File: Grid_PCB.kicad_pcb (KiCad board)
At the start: 2 copper layers, 220 x 20 mm, 31 parts, among them J1 Conn_01x04_Female, J10 LED_Conn, J2 Conn_01x04_Female, J3 Conn_01x04_Female, J4 Conn_01x04_Female, J5 Conn_01x04_Female, J6 Conn_01x04_Female, J7 Conn_01x04_Female, J8 Conn_01x04_Female, J9 ESP_Conn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

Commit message: continued progress
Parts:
- added H1: MountingHole, MountingHole:MountingHole_3.2mm_M3, F.Cu at (179.1, 15.2)
- added H1: MountingHole, MountingHole:MountingHole_3.2mm_M3, F.Cu at (54.6, 3.81)
- moved H2 89.6 mm to (207.0, 3.81)
- moved H1 66.3 mm to (29.2, 15.2)
- moved RN1 64.1 mm to (126.6, 2.54)
- moved J10 13.6 mm to (226.1, 15.5), turned to 0 degrees
- moved C8 9.71 mm to (222.0, 15.2)
- moved J8 9.47 mm to (217.2, 8.73)
- moved D8 9.45 mm to (222.2, 10.2)
- moved J9 8.13 mm to (2.54, 19.1)
- moved TP1 7.62 mm to (22.9, 3.81)
- moved U1 7.62 mm to (19.1, 19.1)
- moved C7 5.36 mm to (196.8, 15.2)
- moved C4 5.35 mm to (120.4, 15.2)
- moved D7 4.99 mm to (196.8, 10.2)
- moved J7 4.70 mm to (191.8, 8.73)
- moved C6 2.60 mm to (171.2, 15.2)
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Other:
- board size 220 x 20 mm -> 228.2 x 20 mm

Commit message: finished first pass at routing
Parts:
- removed the H1 at (179.1, 15.2)
- removed the H1 at (54.6, 3.81)
- removed the H1 at (29.2, 15.2)
- removed RN1: R_Network08(10k), Resistor_THT:R_Array_SIP9
- added H1: MountingHole, MountingHole:MountingHole_3.2mm_M3, F.Cu at (66.8, 88.1)
- added H3: MountingHole, MountingHole:MountingHole_3.2mm_M3, F.Cu at (219.5, 99.6)
- added H4: MountingHole, MountingHole:MountingHole_3.2mm_M3, F.Cu at (244.6, 88.1)
- added R1: 10K, Resistor_SMD:R_0805_2012Metric_Pad1.20x1.40mm_HandSolder, F.Cu at (75.9, 89.4)
- added R2: 10K, Resistor_SMD:R_0805_2012Metric_Pad1.20x1.40mm_HandSolder, F.Cu at (101.3, 89.7)
- added R3: 10K, Resistor_SMD:R_0805_2012Metric_Pad1.20x1.40mm_HandSolder, F.Cu at (126.7, 89.4)
- added R4: 10K, Resistor_SMD:R_0805_2012Metric_Pad1.20x1.40mm_HandSolder, F.Cu at (152.1, 89.4)
- added R5: 10K, Resistor_SMD:R_0805_2012Metric_Pad1.20x1.40mm_HandSolder, F.Cu at (177.5, 89.3)
- added R6: 10K, Resistor_SMD:R_0805_2012Metric_Pad1.20x1.40mm_HandSolder, F.Cu at (202.9, 89.4)
- added R7: 10K, Resistor_SMD:R_0805_2012Metric_Pad1.20x1.40mm_HandSolder, F.Cu at (228.3, 89.4)
- added R8: 10K, Resistor_SMD:R_0805_2012Metric_Pad1.20x1.40mm_HandSolder, F.Cu at (253.7, 89.4)
- J9: footprint Connector_PinHeader_2.54mm:PinHeader_1x08_P2.54mm_Horizontal -> Connector_PinHeader_2.54mm:PinHeader_1x07_P2.54mm_Horizontal
- moved H2 149.7 mm to (91.9, 99.6)
- moved C8 92.1 mm to (260.1, 99.1)
- moved D6 92.1 mm to (209.6, 94.0)
- moved D8 92.1 mm to (260.4, 94.0)
- moved C1 92.1 mm to (82.3, 99.1)
- moved C3 92.1 mm to (133.3, 99.1)
- moved C4 92.1 mm to (158.5, 99.1)
- moved C5 92.1 mm to (184.2, 99.1)
- moved C6 92.1 mm to (209.3, 99.1)
- moved C7 92.1 mm to (234.9, 99.1)
- moved D1 92.1 mm to (82.5, 94.0)
- moved D2 92.1 mm to (108.0, 94.0)
- moved D3 92.1 mm to (133.3, 94.0)
- moved D4 92.1 mm to (158.8, 94.0)
- moved D5 92.1 mm to (184.2, 94.0)
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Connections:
- J10 pad 1: /LED_Out -> /LED_In
- J10 pad 2: /LED_In -> /LED_Out
- J9 pad 2: /MUX_OUT -> /ESPselC
- J9 pad 3: /ESPselA -> /ESPselB
- J9 pad 4: /ESPselB -> /ESPselA
- J9 pad 5: /ESPselC -> /MUX_OUT
- U1 pad 13: /BTN5 -> /BTN6
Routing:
- net VDD: track 0.00 -> 273.0 mm
- net /LED_In: track 0.00 -> 228.6 mm, vias 0 -> 3
- net /BTN7: track 0.00 -> 212.1 mm
- net /BTN6: track 0.00 -> 183.8 mm
- net /BTN5: track 0.00 -> 155.5 mm
- net /BTN4: track 0.00 -> 127.3 mm
- net /BTN3: track 0.00 -> 95.8 mm
- net /BTN2: track 0.00 -> 73.7 mm
- net /BTN1: track 0.00 -> 50.9 mm
- net /BTN0: track 0.00 -> 28.0 mm
- net /InputNode7/DIN: track 0.00 -> 25.5 mm, vias 0 -> 2
- net /InputNode6/DIN: track 0.00 -> 25.5 mm, vias 0 -> 2
- net /InputNode2/DIN: track 0.00 -> 25.5 mm, vias 0 -> 2
- net /LED_Link: track 0.00 -> 25.4 mm, vias 0 -> 2
- net /InputNode3/DIN: track 0.00 -> 25.4 mm, vias 0 -> 2
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- added copper zone on B.Cu, net GND
- added copper zone on F.Cu, net GND
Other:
- outline, holes or cut-outs redrawn
- net class Power added: clearance 0.2, trace_width 0.5, via_dia 0.8, via_drill 0.4

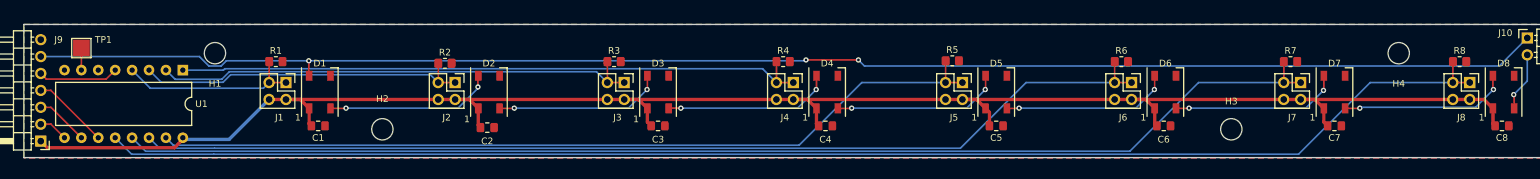
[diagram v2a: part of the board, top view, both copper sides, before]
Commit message: trace update
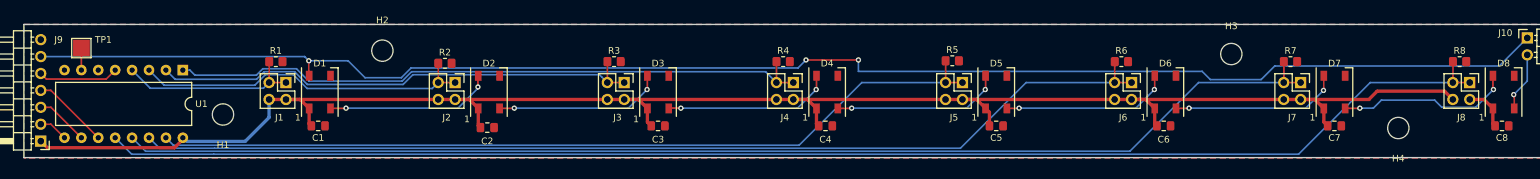
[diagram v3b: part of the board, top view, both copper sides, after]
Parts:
- moved H2 11.8 mm to (91.9, 87.8)
- moved H3 11.3 mm to (219.5, 88.3)
- moved H4 11.2 mm to (244.5, 99.4)
- moved H1 9.29 mm to (68.0, 97.3)
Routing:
- net /LED_In: track 228.6 -> 232.9 mm
- net /BTN3: track 95.8 -> 97.6 mm
- net /BTN2: track 73.7 -> 74.9 mm
- net /BTN1: track 50.9 -> 52.0 mm
- net /InputNode7/DIN: track 25.5 -> 26.6 mm

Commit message: flipped components to back side
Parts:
- removed TP1: TestPoint, TestPoint:TestPoint_Pad_2.5x2.5mm
- added J11: ESP_Conn, Connector_JST:JST_EH_B2B-EH-A_1x02_P2.50mm_Vertical, B.Cu at (46.3, 101.4)
- J10: footprint Connector_PinHeader_2.54mm:PinHeader_1x02_P2.54mm_Horizontal -> Connector_JST:JST_EH_B2B-EH-A_1x02_P2.50mm_Vertical; moved to B.Cu
- J9: footprint Connector_PinHeader_2.54mm:PinHeader_1x07_P2.54mm_Horizontal -> Connector_JST:JST_EH_B5B-EH-A_1x05_P2.50mm_Vertical; moved to B.Cu
- U1: moved to B.Cu
- moved U1 17.3 mm to (45.0, 87.4)
- moved J9 4.37 mm to (41.1, 97.0), turned to 90 degrees
- moved J10 3.97 mm to (260.1, 87.1)
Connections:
- J9 pad 1: VDD -> /ESPselA
- J9 pad 2: /ESPselC -> /ESPselB
- J9 pad 3: /ESPselB -> /ESPselC
- J9 pad 4: /ESPselA -> /MUX_OUT
- J9 pad 5: /MUX_OUT -> /LED_In
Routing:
- net /BTN3: track 97.6 -> 117.4 mm
- net /ESPselC: track 4.40 -> 24.0 mm
- net /BTN4: track 127.3 -> 143.3 mm
- net /BTN2: track 74.9 -> 89.3 mm
- net /ESPselB: track 7.99 -> 20.4 mm
- net /BTN5: track 155.5 -> 167.4 mm
- net /BTN1: track 52.0 -> 60.3 mm
- net /BTN6: track 183.8 -> 191.2 mm
- net /ESPselA: track 11.6 -> 17.3 mm
- net VDD: track 273.4 -> 278.1 mm
- net /BTN0: track 28.0 -> 31.4 mm
- net Net-(U1-Pad7): track 3.30 -> 0.00 mm
- net /MUX_OUT: track 12.1 -> 15.0 mm
- net /LED_In: track 232.9 -> 230.7 mm
- net /BTN7: track 212.1 -> 214.0 mm
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
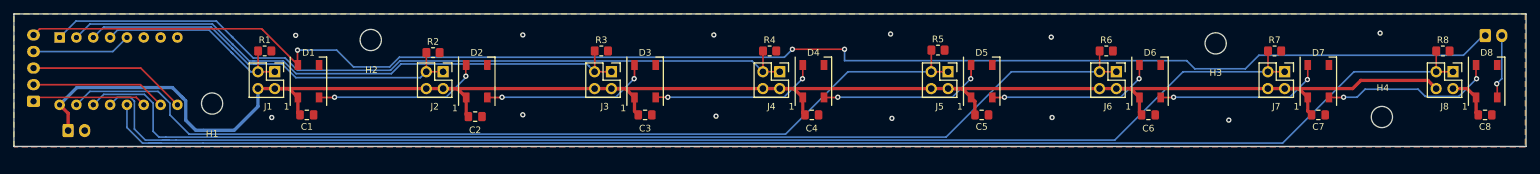
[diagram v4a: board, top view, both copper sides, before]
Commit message: rotated the mux
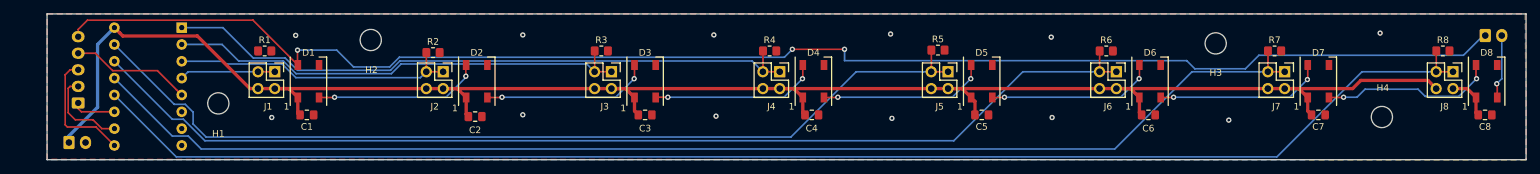
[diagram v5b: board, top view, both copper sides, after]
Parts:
- moved U1 18.5 mm to (63.4, 85.9), turned to 180 degrees
- moved J9 6.75 mm to (47.8, 97.3)
- moved J11 1.81 mm to (46.4, 103.2)
- moved H1 0.94 mm to (68.9, 97.3)
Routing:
- net /BTN3: track 117.4 -> 97.3 mm
- net /BTN2: track 89.3 -> 70.9 mm
- net /BTN0: track 31.4 -> 14.4 mm
- net /BTN1: track 60.3 -> 43.7 mm
- net /ESPselA: track 17.3 -> 6.51 mm
- net /ESPselB: track 20.4 -> 13.3 mm
- net /ESPselC: track 24.0 -> 18.6 mm
- net /LED_In: track 230.7 -> 225.8 mm
- net /BTN5: track 167.4 -> 163.6 mm
- net /BTN4: track 143.3 -> 140.0 mm
- net /MUX_OUT: track 15.0 -> 18.2 mm
- net /BTN6: track 191.2 -> 189.0 mm
- net VDD: track 278.1 -> 279.5 mm
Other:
- board size 228.2 x 20 mm -> 223.2 x 22 mm

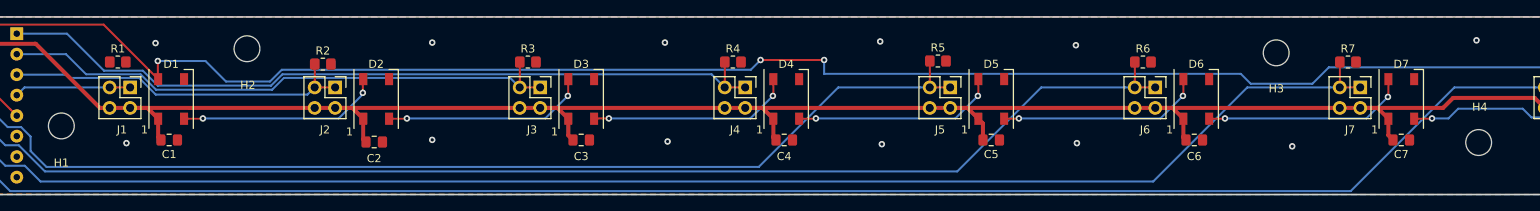
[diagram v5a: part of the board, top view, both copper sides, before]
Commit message: minor silkscreen and mounting hole fix
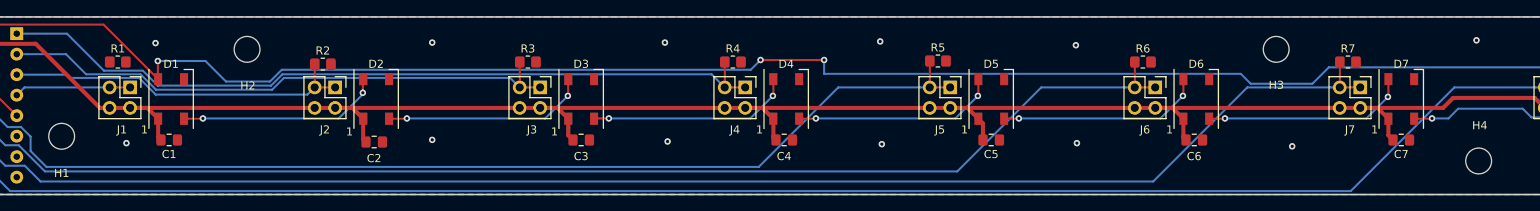
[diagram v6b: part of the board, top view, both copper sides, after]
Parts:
- moved H4 2.29 mm to (244.5, 101.7)
- moved H1 1.28 mm to (69.0, 98.6)
- moved H3 0.43 mm to (219.5, 87.8)
- moved H2 0.08 mm to (92.0, 87.8)

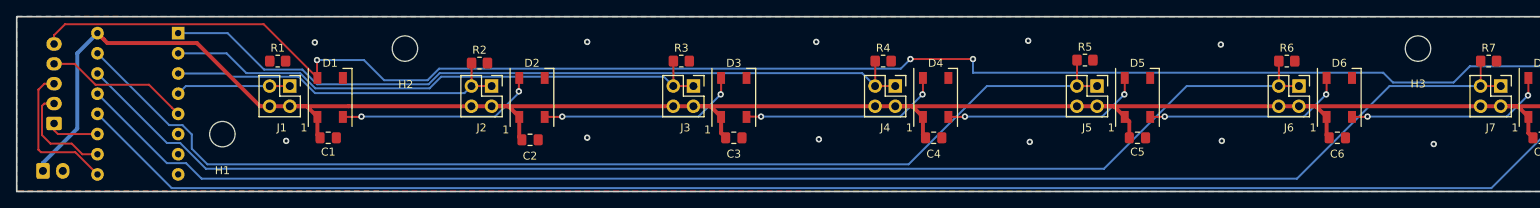
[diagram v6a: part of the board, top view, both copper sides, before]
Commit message: fixed added cap for mux and fixed drc errors
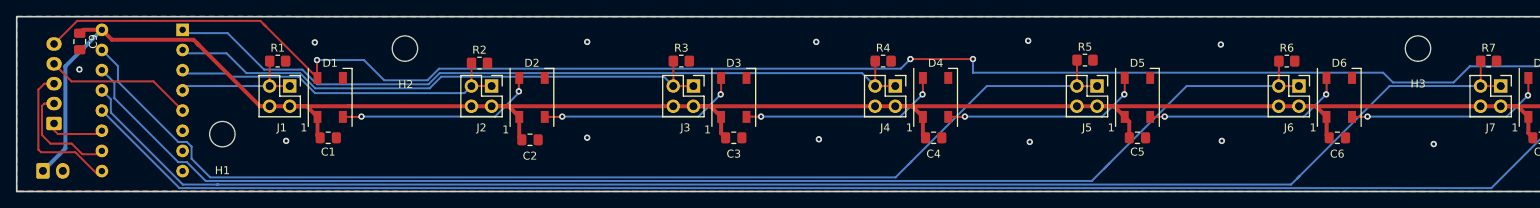
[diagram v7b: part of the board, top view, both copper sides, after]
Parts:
- added C9: 0.1uF, Capacitor_SMD:C_0805_2012Metric_Pad1.18x1.45mm_HandSolder, F.Cu at (51.0, 86.9)
- moved U1 0.70 mm to (64.0, 85.5)
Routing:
- net VDD: track 279.5 -> 283.1 mm
- net /BTN0: track 14.4 -> 17.6 mm
- net /BTN5: track 163.6 -> 166.7 mm
- net /BTN4: track 140.0 -> 142.5 mm
- net /BTN6: track 189.0 -> 190.9 mm
- net GND: vias 12 -> 13

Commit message: finsihed sch and pcb
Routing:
- net VDD: track 283.1 -> 284.2 mm
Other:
- net class Power: trace_width 0.5 -> 0.3683
